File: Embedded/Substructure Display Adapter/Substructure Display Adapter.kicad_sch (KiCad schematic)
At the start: 9 parts, among them J1 HUB75, J2 Input, J3 Output, U1 D0 FFC, U2 74HC245D_653, U3 74HC245D_653

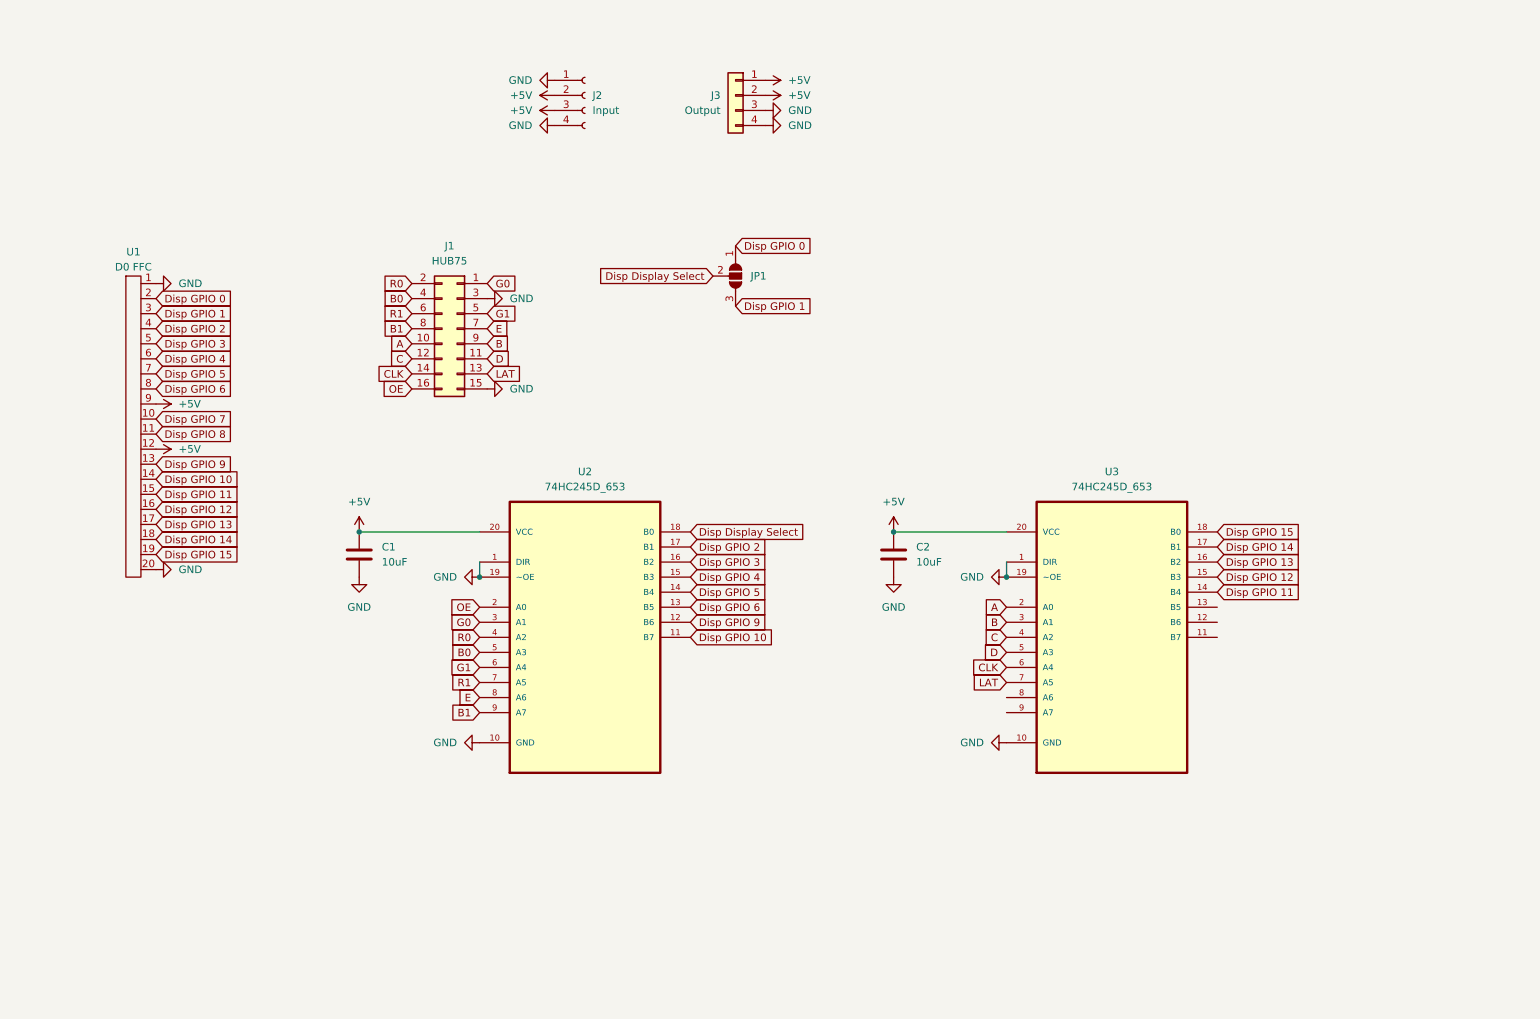
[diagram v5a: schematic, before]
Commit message: Added 2nd Display Adapter (Initial Commit)
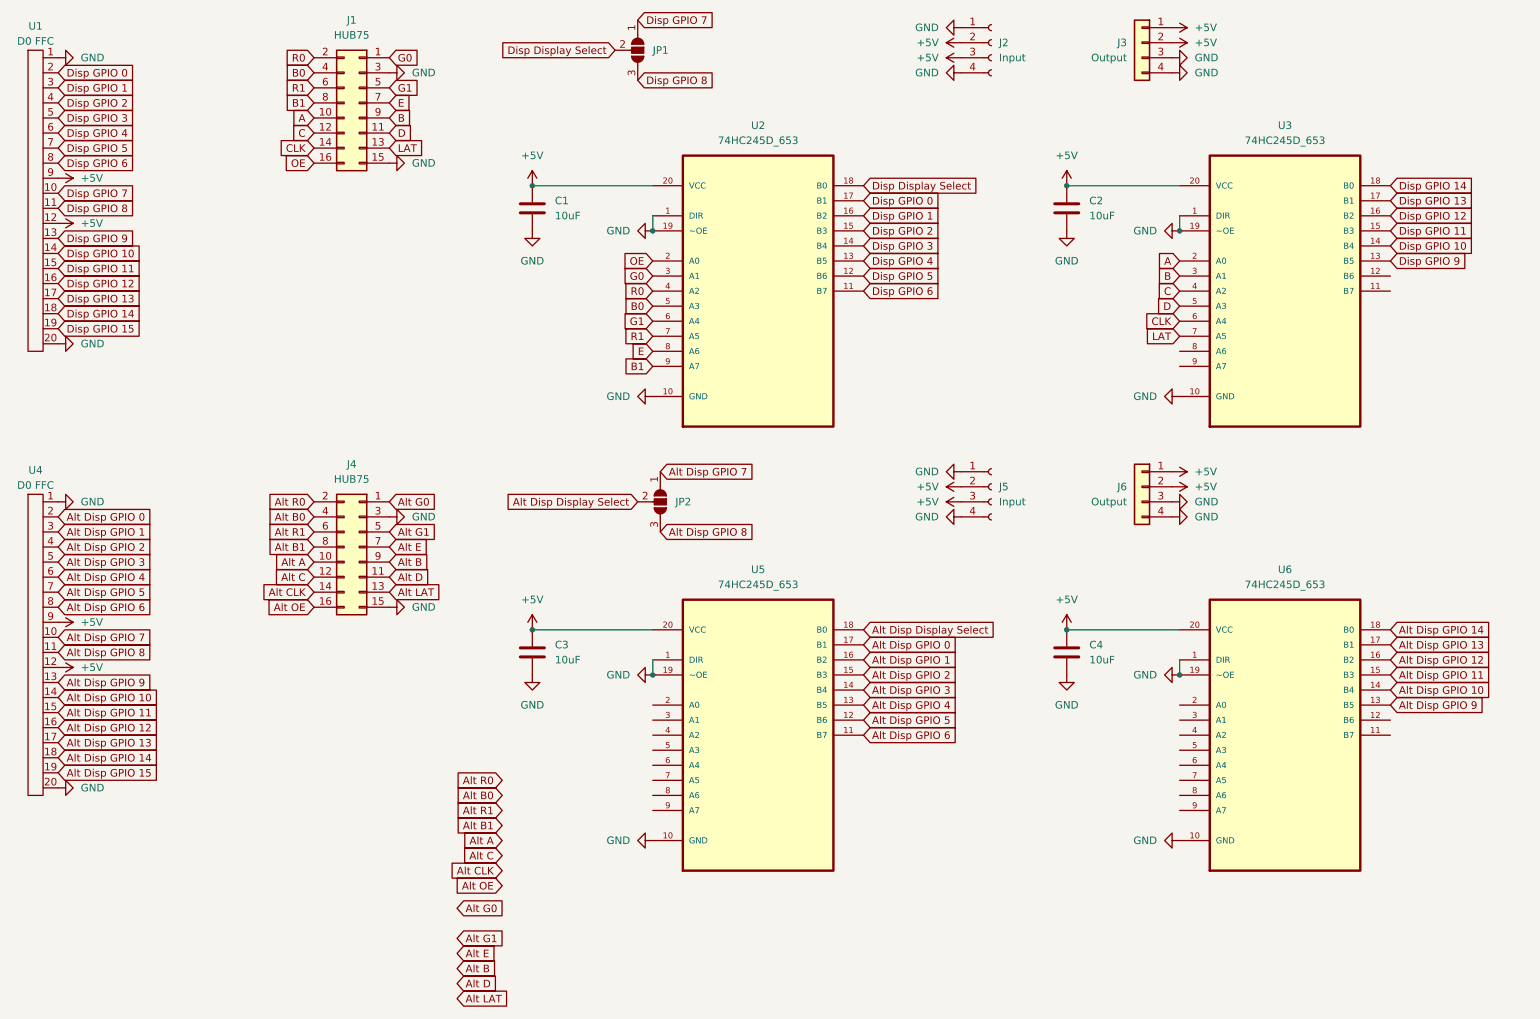
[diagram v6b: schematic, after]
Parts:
- added C3, C4: 10uF, Capacitor_SMD:C_0603_1608Metric_Pad1.08x0.95mm_HandSolder, symbol Device:C
- added J4: HUB75, Connector_PinHeader_2.54mm:PinHeader_2x08_P2.54mm_Vertical, symbol Connector_Generic:Conn_02x08_Odd_Even
- added J5: Input, Connector_JST:JST_XH_S4B-XH-A_1x04_P2.50mm_Horizontal, symbol Connector:Conn_01x04_Socket
- added J6: Output, Connector_JST:JST_VH_B4P-VH-B_1x04_P3.96mm_Vertical, symbol Connector_Generic:Conn_01x04
- added JP2: SolderJumper_3_Open, Jumper:SolderJumper-3_P1.3mm_Open_RoundedPad1.0x1.5mm_NumberLabels, symbol Jumper:SolderJumper_3_Open
- added U4: D0 FFC, FFC:FFC 0.8mm 20P, symbol FFC:FFC-20
- added U5, U6: 74HC245D_653, 74HC245D:SOIC127P1032X265-20N, symbol 74HC245:74HC245D_653
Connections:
- net +5V: now also C3.1, C4.1, J5.2 (Pin_2), J5.3 (Pin_3), J6.1 (Pin_1), J6.2 (Pin_2), U4.12, U4.9, U5.20 (VCC), U6.20 (VCC)
- net Disp GPIO 0: now also U2.17 (B1); no longer JP1.1 (A)
- net Disp GPIO 1: now also U2.16 (B2); no longer JP1.3 (B)
- net Disp GPIO 10: now also U3.14 (B4); no longer U2.11 (B7)
- net Disp GPIO 11: now also U3.15 (B3); no longer U3.14 (B4)
- net Disp GPIO 12: now also U3.16 (B2); no longer U3.15 (B3)
- net Disp GPIO 13: now also U3.17 (B1); no longer U3.16 (B2)
- net Disp GPIO 14: now also U3.18 (B0); no longer U3.17 (B1)
- net Disp GPIO 15: no longer U3.18 (B0)
- net Disp GPIO 2: now also U2.15 (B3); no longer U2.17 (B1)
- net Disp GPIO 3: now also U2.14 (B4); no longer U2.16 (B2)
- net Disp GPIO 4: now also U2.13 (B5); no longer U2.15 (B3)
- net Disp GPIO 5: now also U2.12 (B6); no longer U2.14 (B4)
- net Disp GPIO 6: now also U2.11 (B7); no longer U2.13 (B5)
- net Disp GPIO 7: now also JP1.1 (A)
- net Disp GPIO 8: now also JP1.3 (B)
- net Disp GPIO 9: now also U3.13 (B5); no longer U2.12 (B6)
- net GND: now also C3.2, C4.2, J4.15 (Pin_15), J4.3 (Pin_3), J5.1 (Pin_1), J5.4 (Pin_4), J6.3 (Pin_3), J6.4 (Pin_4), U4.1, U4.20, U5.1 (DIR), U5.10 (GND), U5.19 (~OE), U6.1 (DIR), U6.10 (GND), U6.19 (~OE)
- new net Alt A: J4.10 (Pin_10)
- new net Alt B: J4.9 (Pin_9)
- new net Alt B0: J4.4 (Pin_4)
- new net Alt B1: J4.8 (Pin_8)
- new net Alt C: J4.12 (Pin_12)
- new net Alt CLK: J4.14 (Pin_14)
- new net Alt D: J4.11 (Pin_11)
- new net Alt Disp Display Select: JP2.2 (C), U5.18 (B0)
- new net Alt Disp GPIO 0: U4.2, U5.17 (B1)
- new net Alt Disp GPIO 1: U4.3, U5.16 (B2)
- new net Alt Disp GPIO 10: U4.14, U6.14 (B4)
- new net Alt Disp GPIO 11: U4.15, U6.15 (B3)
- new net Alt Disp GPIO 12: U4.16, U6.16 (B2)
- new net Alt Disp GPIO 13: U4.17, U6.17 (B1)
- new net Alt Disp GPIO 14: U4.18, U6.18 (B0)
- new net Alt Disp GPIO 15: U4.19
- new net Alt Disp GPIO 2: U4.4, U5.15 (B3)
- new net Alt Disp GPIO 3: U4.5, U5.14 (B4)
- new net Alt Disp GPIO 4: U4.6, U5.13 (B5)
- new net Alt Disp GPIO 5: U4.7, U5.12 (B6)
- new net Alt Disp GPIO 6: U4.8, U5.11 (B7)
- new net Alt Disp GPIO 7: JP2.1 (A), U4.10
- new net Alt Disp GPIO 8: JP2.3 (B), U4.11
- new net Alt Disp GPIO 9: U4.13, U6.13 (B5)
- new net Alt E: J4.7 (Pin_7)
- new net Alt G0: J4.1 (Pin_1)
- new net Alt G1: J4.5 (Pin_5)
- new net Alt LAT: J4.13 (Pin_13)
- new net Alt OE: J4.16 (Pin_16)
- new net Alt R0: J4.2 (Pin_2)
- new net Alt R1: J4.6 (Pin_6)
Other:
- moved on the sheet: C1, C2, J1, J2, J3, JP1, U1, U2, U3

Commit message: Added Component placement ideation
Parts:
- U4: footprint FFC:FFC 0.8mm 20P -> FCC:FFC 0.8mm 20P
- U5, U6: footprint 74HC245D:SOIC127P1032X265-20N -> 74HC245:SOIC127P1032X265-20N
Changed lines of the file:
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@@
 			)
 		)
-		(property "Footprint" "74HC245D:SOIC127P1032X265-20N"
+		(property "Footprint" "74HC245:SOIC127P1032X265-20N"
 			(at 232.41 138.43 0)
 			(effects
@@
 			)
 		)
-		(property "Footprint" "74HC245D:SOIC127P1032X265-20N"
+		(property "Footprint" "74HC245:SOIC127P1032X265-20N"
 			(at 143.51 138.43 0)
 			(effects
@@
 			)
 		)
-		(property "Footprint" "FFC:FFC 0.8mm 20P"
+		(property "Footprint" "FCC:FFC 0.8mm 20P"
 			(at 21.59 125.73 0)
 			(effects

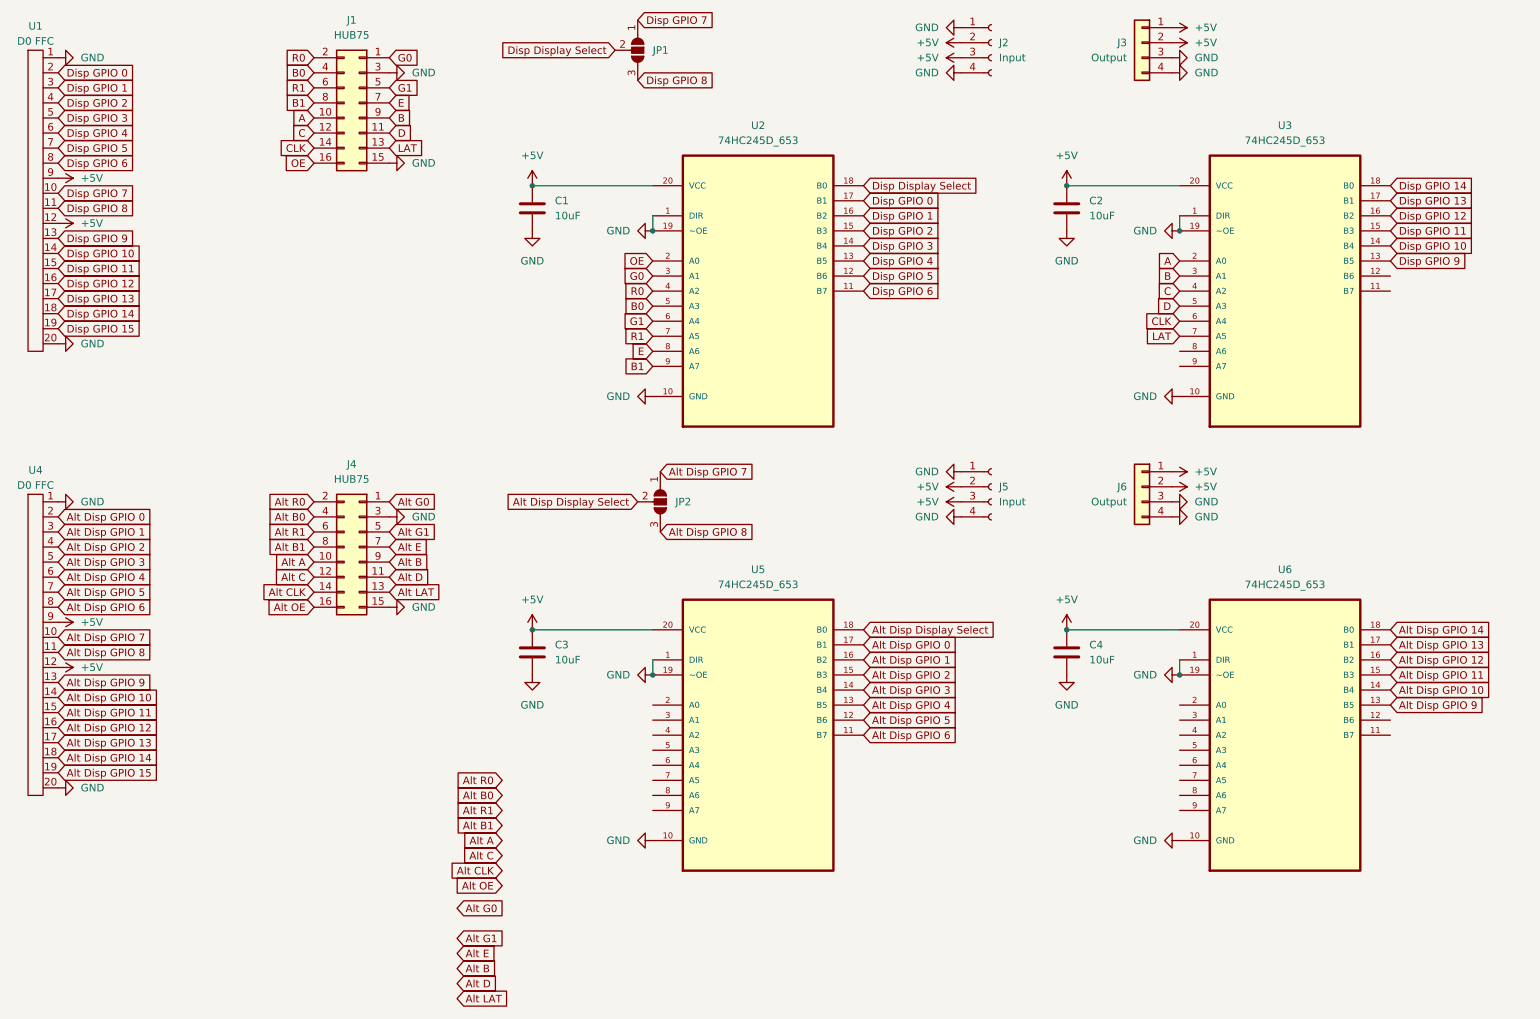
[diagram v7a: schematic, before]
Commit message: Modified Pin orientation for 2nd Adapter
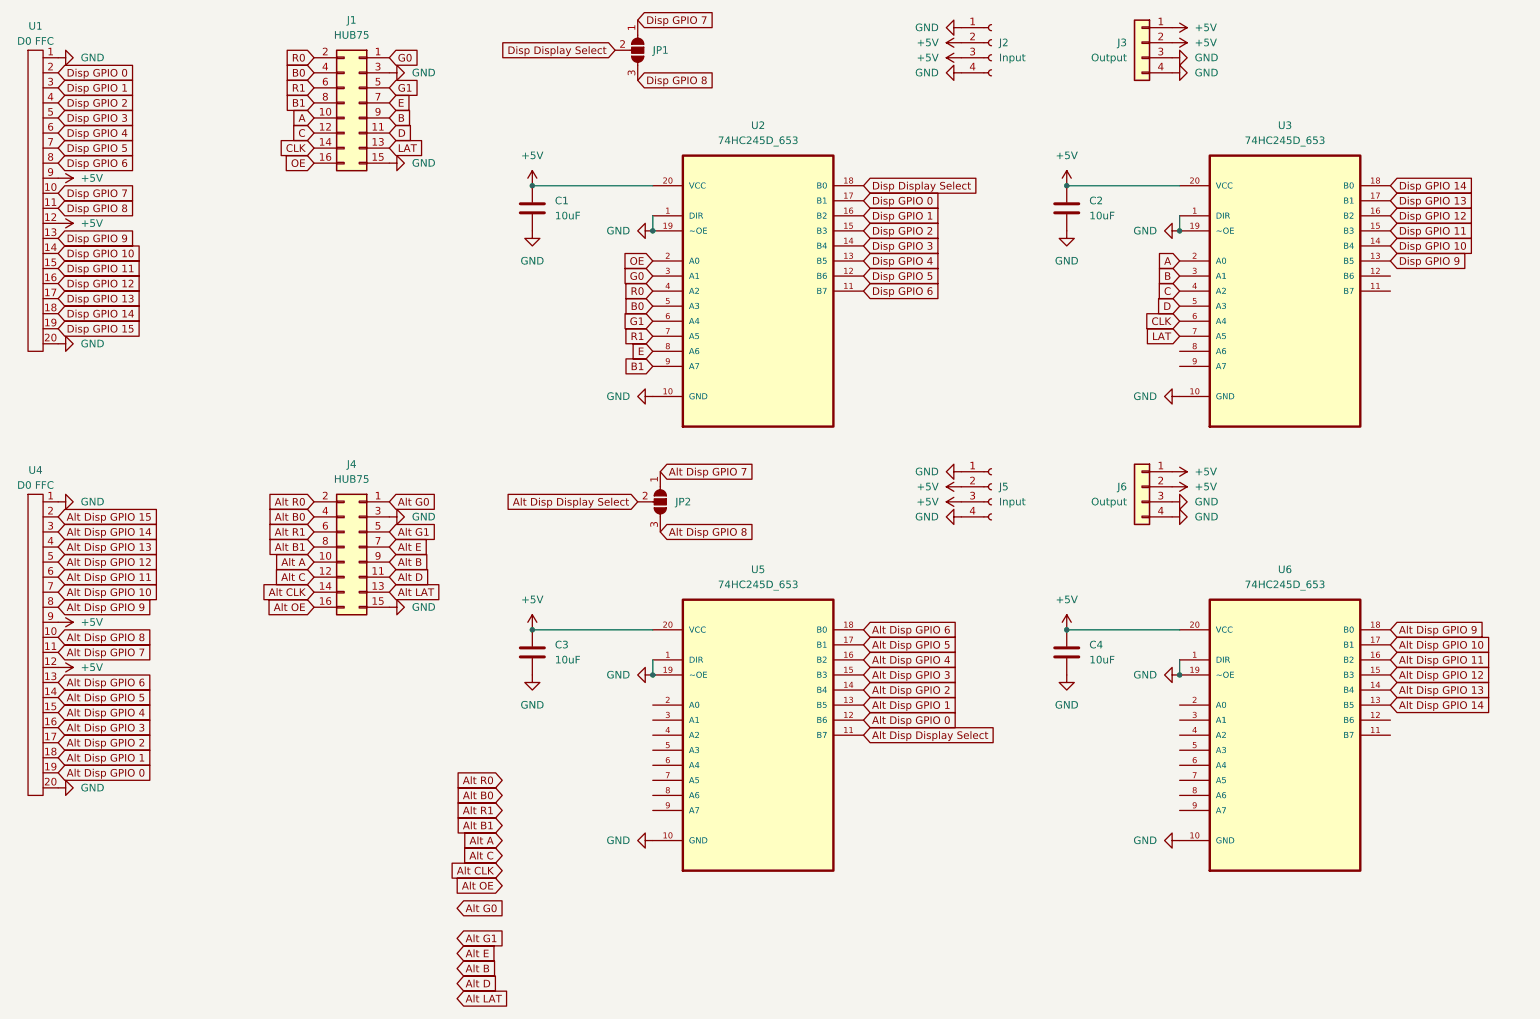
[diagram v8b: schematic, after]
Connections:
- net Alt Disp Display Select: now also U5.11 (B7); no longer U5.18 (B0)
- net Alt Disp GPIO 0: now also U4.19, U5.12 (B6); no longer U4.2, U5.17 (B1)
- net Alt Disp GPIO 1: now also U4.18, U5.13 (B5); no longer U4.3, U5.16 (B2)
- net Alt Disp GPIO 10: now also U4.7, U6.17 (B1); no longer U4.14, U6.14 (B4)
- net Alt Disp GPIO 11: now also U4.6, U6.16 (B2); no longer U4.15, U6.15 (B3)
- net Alt Disp GPIO 12: now also U4.5, U6.15 (B3); no longer U4.16, U6.16 (B2)
- net Alt Disp GPIO 13: now also U4.4, U6.14 (B4); no longer U4.17, U6.17 (B1)
- net Alt Disp GPIO 14: now also U4.3, U6.13 (B5); no longer U4.18, U6.18 (B0)
- net Alt Disp GPIO 15: now also U4.2; no longer U4.19
- net Alt Disp GPIO 2: now also U4.17, U5.14 (B4); no longer U4.4, U5.15 (B3)
- net Alt Disp GPIO 3: now also U4.16, U5.15 (B3); no longer U4.5, U5.14 (B4)
- net Alt Disp GPIO 4: now also U4.15, U5.16 (B2); no longer U4.6, U5.13 (B5)
- net Alt Disp GPIO 5: now also U4.14, U5.17 (B1); no longer U4.7, U5.12 (B6)
- net Alt Disp GPIO 6: now also U4.13, U5.18 (B0); no longer U4.8, U5.11 (B7)
- net Alt Disp GPIO 7: now also U4.11; no longer U4.10
- net Alt Disp GPIO 8: now also U4.10; no longer U4.11
- net Alt Disp GPIO 9: now also U4.8, U6.18 (B0); no longer U4.13, U6.13 (B5)
